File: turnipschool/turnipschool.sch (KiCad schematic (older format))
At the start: 63 parts, among them J1 USB-DEVICE-SHIELD, P1 CONN_1, P10 CONN_1, P11 CONN_1, P2 RESET_N, P3 DD, P4 DC, P5 3V3, P6 GND, P7 CONN_1, P8 CONN_1, P9 CONN_1, T1 BALUN, U1 CC1111, U2 AP7313, U3 USB2412, U4 AP2511SN-7, X1 CRYSTAL, X2 CRYSTAL

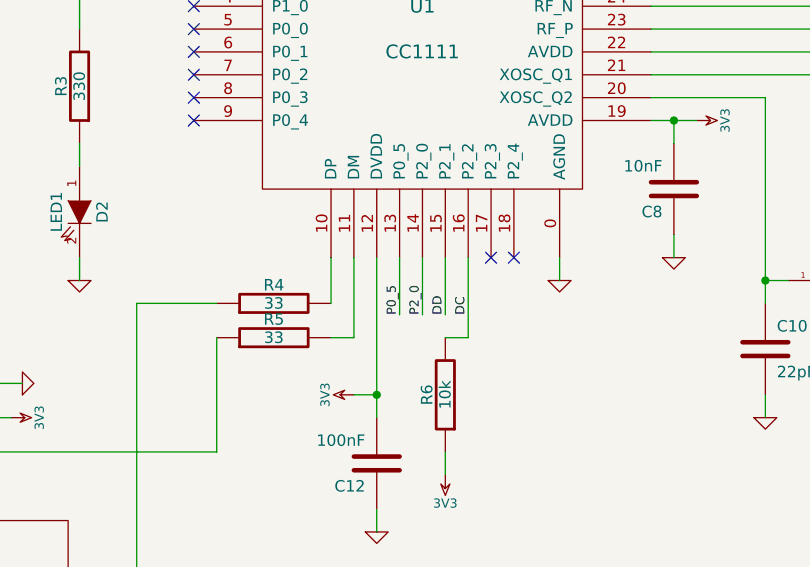
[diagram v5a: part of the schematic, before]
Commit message: fixed some ERC errors
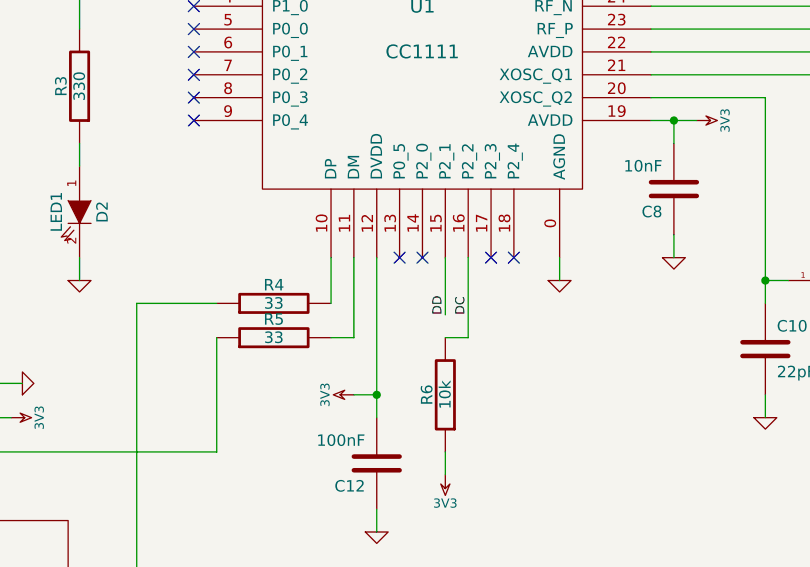
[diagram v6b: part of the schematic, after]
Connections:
- net P0_5: no longer names the net of U1.13 (P0_5)
- net P2_0: no longer names the net of U1.14 (P2_0)
- no-connect marks 21 -> 23

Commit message: modules
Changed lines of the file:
@@
-EESchema Schematic File Version 2  date Wed 25 Jun 2014 12:24:09 AM MDT
+EESchema Schematic File Version 2  date Wed 25 Jun 2014 01:48:25 AM MDT
 LIBS:power
 LIBS:device
@@
 LIBS:valves
 LIBS:cc1111
+LIBS:usb2412
 LIBS:turnipschool-cache
 EELAYER 27 0
@@
 	4550 3300 4550 3200
 Wire Wire Line
-	9050 4050 9900 4050
+	9050 4050 9300 4050
+Wire Wire Line
+	9300 4050 9900 4050
 Wire Wire Line
 	4550 3800 4550 3700
 Connection ~ 6000 1400
 Wire Wire Line
-	5700 1400 6150 1400
+	5700 1400 6000 1400
+Wire Wire Line
+	6000 1400 6150 1400
 Connection ~ 9300 4050
 Wire Wire Line
@@
 Connection ~ 9800 4150
 Wire Wire Line
-	9700 4150 9900 4150
-Wire Wire Line
-	7050 2400 7850 2400
+	9700 4150 9800 4150
+Wire Wire Line
+	9800 4150 9900 4150
+Wire Wire Line
+	7050 2400 7750 2400
+Wire Wire Line
+	7750 2400 7850 2400
 Wire Wire Line
 	8700 3700 8700 3600
 Wire Wire Line
-	8700 2800 8700 3200
-Wire Wire Line
-	7550 3000 7550 3900
+	8700 2800 8700 3100
+Wire Wire Line
+	8700 3100 8700 3200
+Wire Wire Line
+	7550 3000 7550 3800
+Wire Wire Line
+	7550 3800 7550 3900
 Wire Wire Line
 	7550 3000 7050 3000
@@
 	6550 1600 6550 1500
 Wire Wire Line
-	6350 1600 6650 1600
+	6350 1600 6450 1600
+Wire Wire Line
+	6450 1600 6550 1600
+Wire Wire Line
+	6550 1600 6650 1600
 Wire Wire Line
 	6350 1600 6350 1700
@@
 	8800 2750 8900 2750
 Wire Wire Line
-	7050 3100 7250 3100
+	7050 3100 7150 3100
+Wire Wire Line
+	7150 3100 7250 3100
 Wire Wire Line
 	7650 3800 7550 3800
@@
 	5750 4300 5850 4300
 Wire Wire Line
-	5850 3700 5850 4400
+	5850 3700 5850 4300
+Wire Wire Line
+	5850 4300 5850 4400
 Connection ~ 5850 4300
 Wire Wire Line
@@
 	8150 1900 8150 2000
 Wire Wire Line
-	7050 2500 8250 2500
+	7050 2500 8150 2500
+Wire Wire Line
+	8150 2500 8250 2500
 Wire Wire Line
 	8150 2400 8150 2500
@@
 	4650 2200 4750 2200
 Wire Wire Line
-	4750 2100 4750 2400
+	4750 2100 4750 2200
+Wire Wire Line
+	4750 2200 4750 2400
 Wire Wire Line
 	4750 2400 5050 2400
@@
 	4950 7150 4850 7150
 Wire Wire Line
-	4550 7050 4950 7050
+	4550 7050 4850 7050
+Wire Wire Line
+	4850 7050 4950 7050
 Wire Wire Line
 	6650 5800 6650 6000
@@
 	1750 5150 1750 5100
 Wire Wire Line
-	1900 5850 2500 5850
+	1900 5850 1950 5850
+Wire Wire Line
+	1950 5850 2500 5850
 Wire Wire Line
 	1950 5950 1950 5850
@@
 	2500 5750 1000 5750
 Wire Wire Line
-	1000 5650 1000 5850
+	1000 5650 1000 5750
+Wire Wire Line
+	1000 5750 1000 5850
 Connection ~ 1000 5750
 Wire Wire Line
@@
 	3150 3150 3150 3050
 Wire Wire Line
-	6050 7150 6800 7150
+	6050 7150 6300 7150
+Wire Wire Line
+	6300 7150 6650 7150
+Wire Wire Line
+	6650 7150 6800 7150
 Wire Wire Line
 	6800 7150 6800 5800
@@
 	8900 5500 8900 5600
 Wire Wire Line
-	1350 3500 2350 3500
+	1350 3500 2050 3500
+Wire Wire Line
+	2050 3500 2350 3500
 Wire Wire Line
 	1600 3600 1350 3600
@@
 $EndComp
 Wire Wire Line
-	8150 2900 8150 3900
+	8150 2900 8150 3800
+Wire Wire Line
+	8150 3800 8150 3900
 Wire Wire Line
 	8150 2900 7050 2900
@@
 	3500 4100 3750 4100
 Wire Wire Line
-	3750 4100 3750 3550
+	3750 4100 3750 3900
+Wire Wire Line
+	3750 3900 3750 3650
+Wire Wire Line
+	3750 3650 3750 3550
 Wire Wire Line
 	3400 4100 3150 4100
 Wire Wire Line
-	3150 4100 3150 3550
+	3150 4100 3150 3900
+Wire Wire Line
+	3150 3900 3150 3650
+Wire Wire Line
+	3150 3650 3150 3550
 Wire Wire Line
 	3650 3900 3750 3900

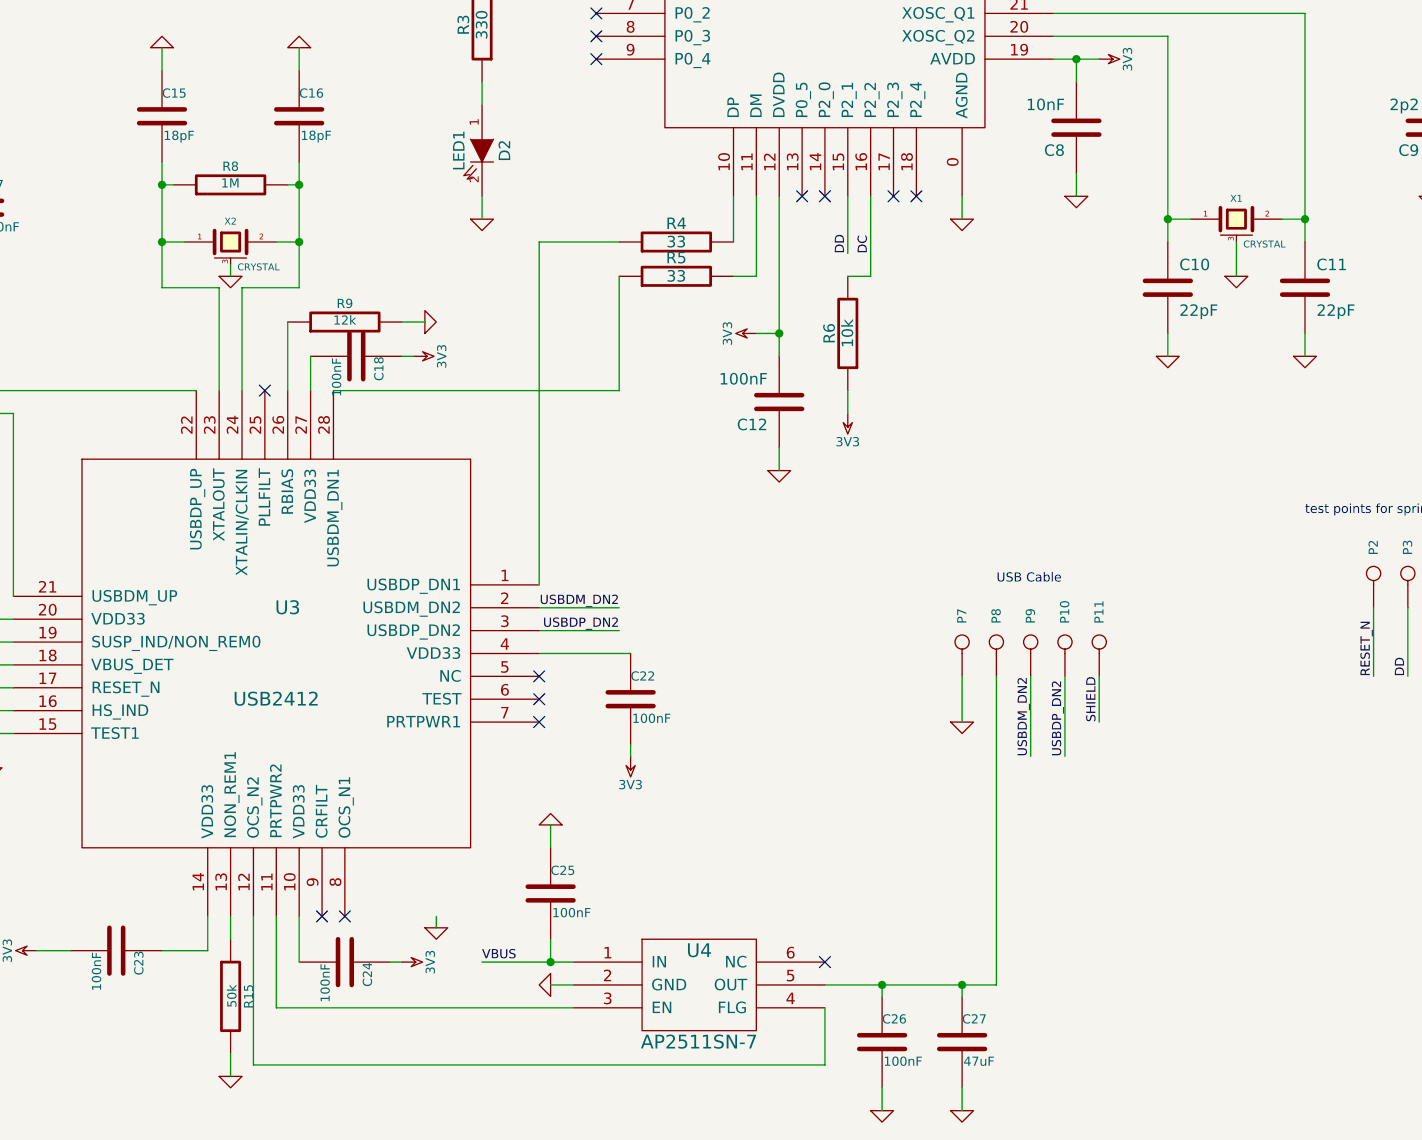
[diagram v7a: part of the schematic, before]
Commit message: 50 mil header for downstream cable
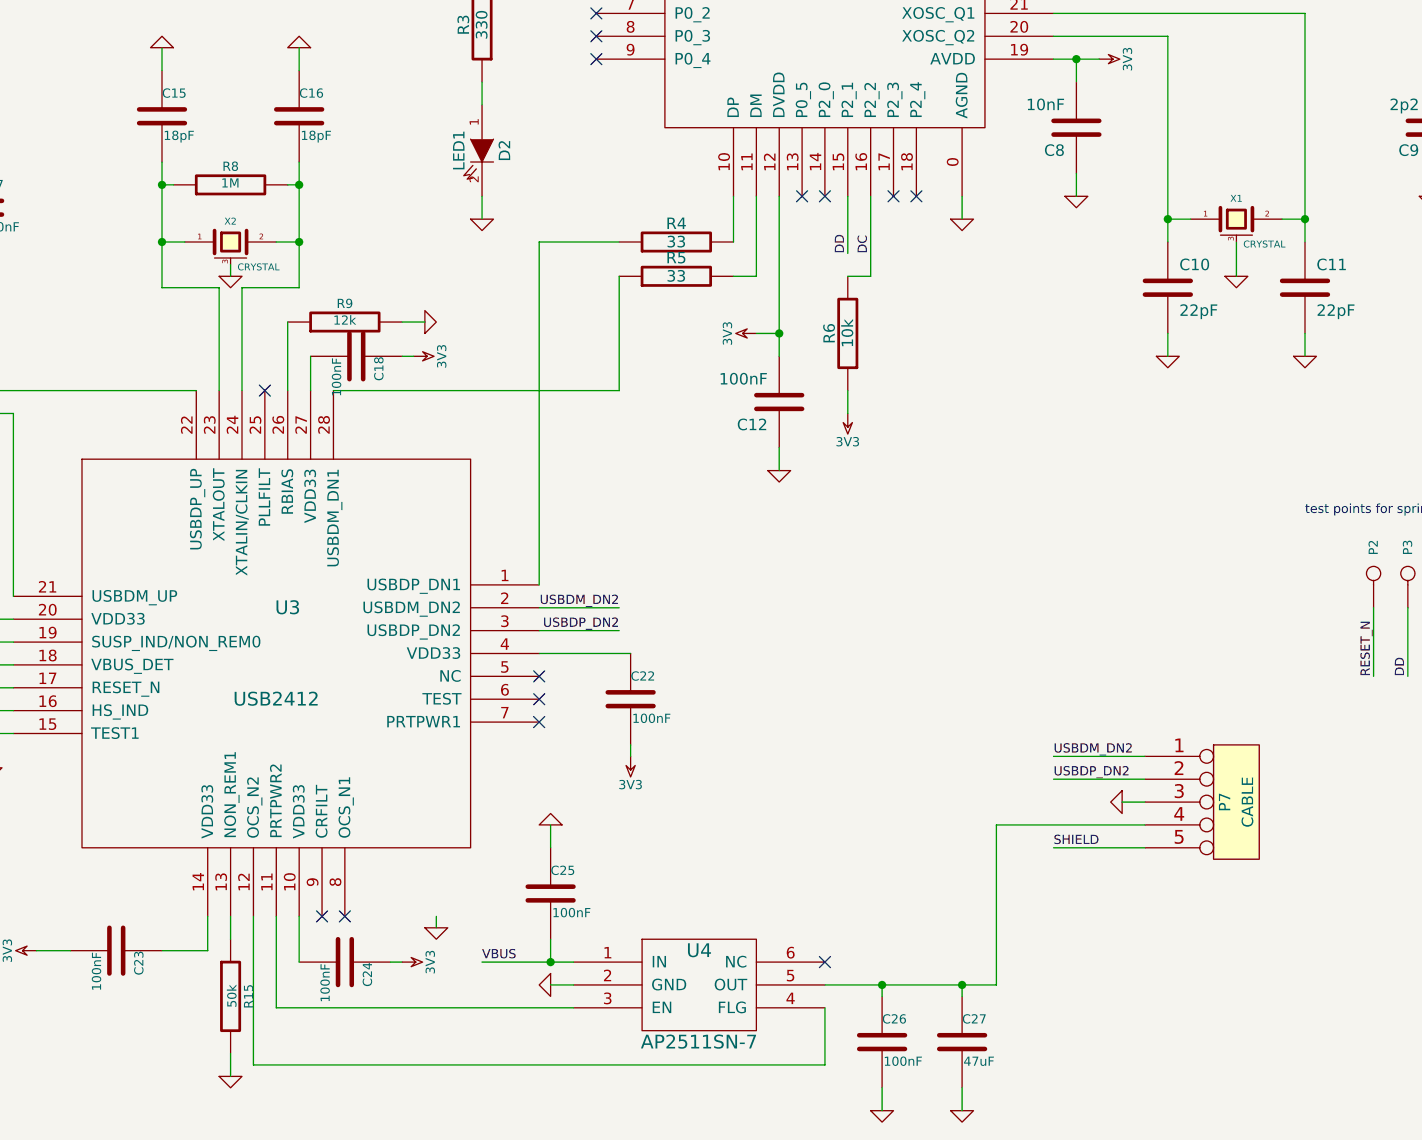
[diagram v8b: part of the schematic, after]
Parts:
- removed P10, P11, P7, P8, P9: CONN_1, symbol CONN_1
- added P7: CABLE, symbol CONN_5
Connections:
- net GND: now also P7.3
- net SHIELD: now also P7.5
- net USBDM_DN2: now also P7.1
- net USBDP_DN2: now also P7.2
- net at C26.1, C27.1, U4.5 (OUT): now also P7.4
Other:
- note removed: "USB Cable"
